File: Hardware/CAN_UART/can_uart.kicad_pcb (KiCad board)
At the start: 4 copper layers, 70 x 67.5 mm, 2 parts, among them J1 Conn_02x23_Odd_Even, J3 Conn_02x23_Odd_Even

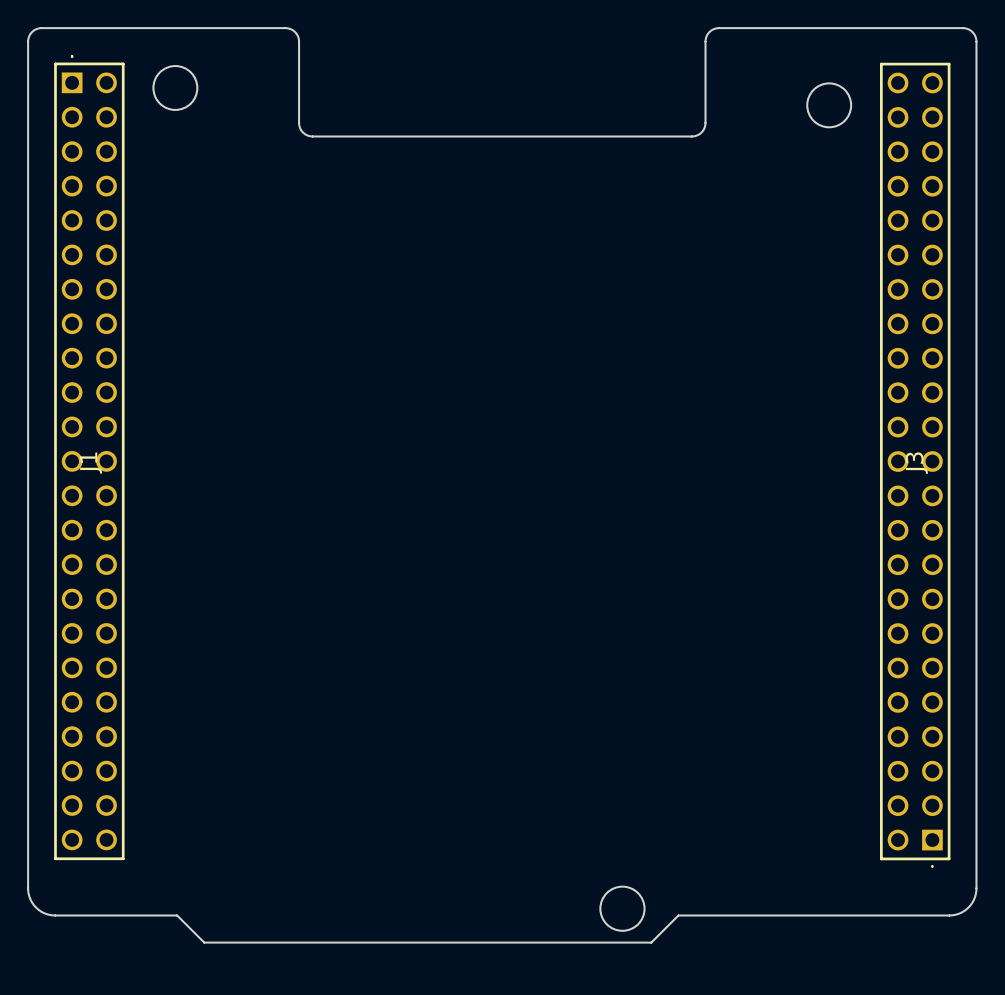
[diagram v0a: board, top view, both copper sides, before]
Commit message: analog & can finished
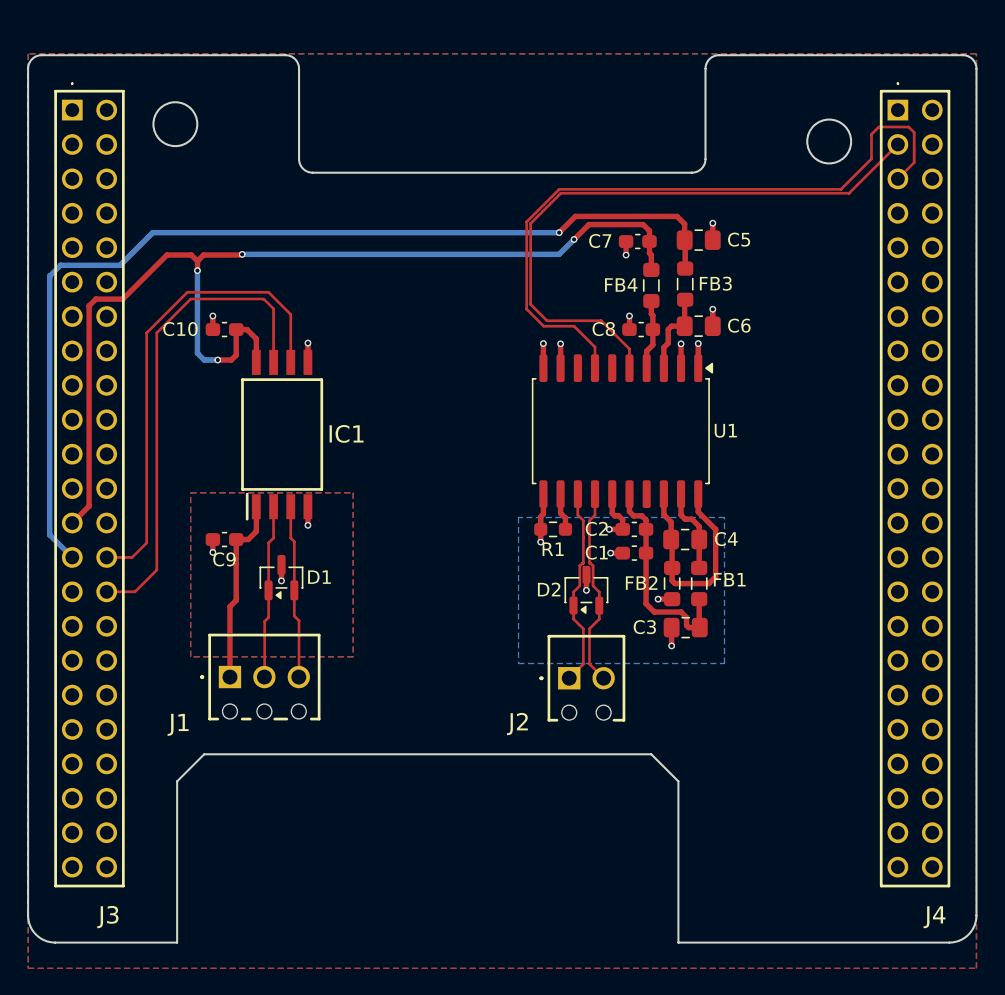
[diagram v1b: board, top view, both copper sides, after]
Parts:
- added C1: 100n, Capacitor_SMD:C_0603_1608Metric_Pad1.08x0.95mm_HandSolder, F.Cu at (160.8, 87.2)
- added C10: 100n, Capacitor_SMD:C_0603_1608Metric_Pad1.08x0.95mm_HandSolder, F.Cu at (130.5, 70.8)
- added C2: 10n, Capacitor_SMD:C_0603_1608Metric_Pad1.08x0.95mm_HandSolder, F.Cu at (160.8, 85.5)
- added C3: 47u, Capacitor_SMD:C_0805_2012Metric_Pad1.18x1.45mm_HandSolder, F.Cu at (164.5, 92.8)
- added C4: 47u, Capacitor_SMD:C_0805_2012Metric_Pad1.18x1.45mm_HandSolder, F.Cu at (164.5, 86.2)
- added C5: 47u, Capacitor_SMD:C_0805_2012Metric_Pad1.18x1.45mm_HandSolder, F.Cu at (165.5, 64.2)
- added C6: 47u, Capacitor_SMD:C_0805_2012Metric_Pad1.18x1.45mm_HandSolder, F.Cu at (165.5, 70.5)
- added C7: 100n, Capacitor_SMD:C_0603_1608Metric_Pad1.08x0.95mm_HandSolder, F.Cu at (161.0, 64.2)
- added C8: 10n, Capacitor_SMD:C_0603_1608Metric_Pad1.08x0.95mm_HandSolder, F.Cu at (161.2, 70.8)
- added C9: 100n, Capacitor_SMD:C_0603_1608Metric_Pad1.08x0.95mm_HandSolder, F.Cu at (130.5, 86.2)
- added D1: SP0502BAHT, Package_TO_SOT_SMD:SOT-23, F.Cu at (134.7, 89.1)
- added D2: PESD5V0L2BT,215, Package_TO_SOT_SMD:SOT-23-3, F.Cu at (157.2, 90.0)
- added FB1: 2K@100MHz, Inductor_SMD:L_0805_2012Metric_Pad1.05x1.20mm_HandSolder, F.Cu at (165.5, 89.5)
- added FB2: 2K@100MHz, Inductor_SMD:L_0805_2012Metric_Pad1.05x1.20mm_HandSolder, F.Cu at (163.5, 89.5)
- added FB3: 2K@100MHz, Inductor_SMD:L_0805_2012Metric_Pad1.05x1.20mm_HandSolder, F.Cu at (164.5, 67.4)
- added FB4: 2K@100MHz, Inductor_SMD:L_0805_2012Metric_Pad1.05x1.20mm_HandSolder, F.Cu at (162.0, 67.5)
- added IC1: ISO7721FQDWVRQ1, PLC_STM:SOIC127P1150X280-8N, F.Cu at (134.8, 78.5)
- added J2: CAN, PLC_STM:1725656, F.Cu at (155.9, 96.5)
- added J4: NUCLEO RIGHT, PLC_STM:PRT12790, F.Cu at (180.2, 54.5)
- added R1: 100k, Resistor_SMD:R_0603_1608Metric_Pad0.98x0.95mm_HandSolder, F.Cu at (154.8, 85.5)
- added U1: ADM3057ExRW, Package_SO:SOIC-20W_7.5x12.8mm_P1.27mm, F.Cu at (159.8, 78.2)
- J1: value Conn_02x23_Odd_Even -> UART; footprint PLC_STM_Power:PRT12790 -> PLC_STM:1725669
- J3: value Conn_02x23_Odd_Even -> NUCLEO LEFT; footprint PLC_STM_Power:PRT12790 -> PLC_STM:PRT12790
- moved J3 83.3 mm to (119.3, 54.5), turned to -90 degrees
- moved J1 45.4 mm to (130.9, 96.4), turned to 0 degrees
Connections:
- J1 pad 1: unconnected-(J1-Pin_1-Pad1) -> +3V
- J1 pad 2: unconnected-(J1-Pin_2-Pad2) -> O_UART_TX
- J1 pad 3: unconnected-(J1-Pin_3-Pad3) -> O_UART_RX
- J3 pad 20: unconnected-(J3-Pin_20-Pad20) -> GND
- J3 pad 22: unconnected-(J3-Pin_22-Pad22) -> GND
- J3 pad 25: unconnected-(J3-Pin_25-Pad25) -> +3V3
- J3 pad 27: unconnected-(J3-Pin_27-Pad27) -> +5V
- J3 pad 28: unconnected-(J3-Pin_28-Pad28) -> UART_TX
- J3 pad 30: unconnected-(J3-Pin_30-Pad30) -> UART_RX
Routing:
- net +3V3: track 0.00 -> 79.3 mm, vias 0 -> 4
- net +5V: track 0.00 -> 73.6 mm, vias 0 -> 1
- net CAN_TX: track 0.00 -> 50.9 mm
- net CAN_RX: track 0.00 -> 45.6 mm
- net UART_RX: track 0.00 -> 35.8 mm
- net UART_TX: track 0.00 -> 35.0 mm
- net /can/GNDISO: track 0.00 -> 16.8 mm
- net /can/VISOIN: track 0.00 -> 16.1 mm
- net CAN_P: track 0.00 -> 14.8 mm
- net CAN_N: track 0.00 -> 14.8 mm
- net GND: track 0.00 -> 14.1 mm, vias 0 -> 10
- net +3V: track 0.00 -> 13.9 mm
- net O_UART_TX: track 0.00 -> 12.9 mm
- net O_UART_RX: track 0.00 -> 12.9 mm
- net CAN_GND_ISO: track 0.00 -> 12.1 mm, vias 0 -> 6
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- added copper zone on B.Cu, net CAN_GND_ISO
- added copper zone on B.Cu, net GND
- added copper zone on F.Cu, net GND
- added copper zone on In1.Cu, net GND
- added copper zone on In2.Cu, net GND
- added copper zone on B.Cu, net GNDREF
- added copper zone on F.Cu, net GNDREF
- added copper zone on In1.Cu, net GNDREF
- added copper zone on In2.Cu, net GNDREF
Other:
- board size 70 x 67.5 mm -> 70 x 65.5 mm
- board text removed: "®©®"
